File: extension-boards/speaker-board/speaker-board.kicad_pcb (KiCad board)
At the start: 2 copper layers, 60 x 40 mm, 14 parts, among them J1 Conn_02x04_Odd_Even, U1 LM386

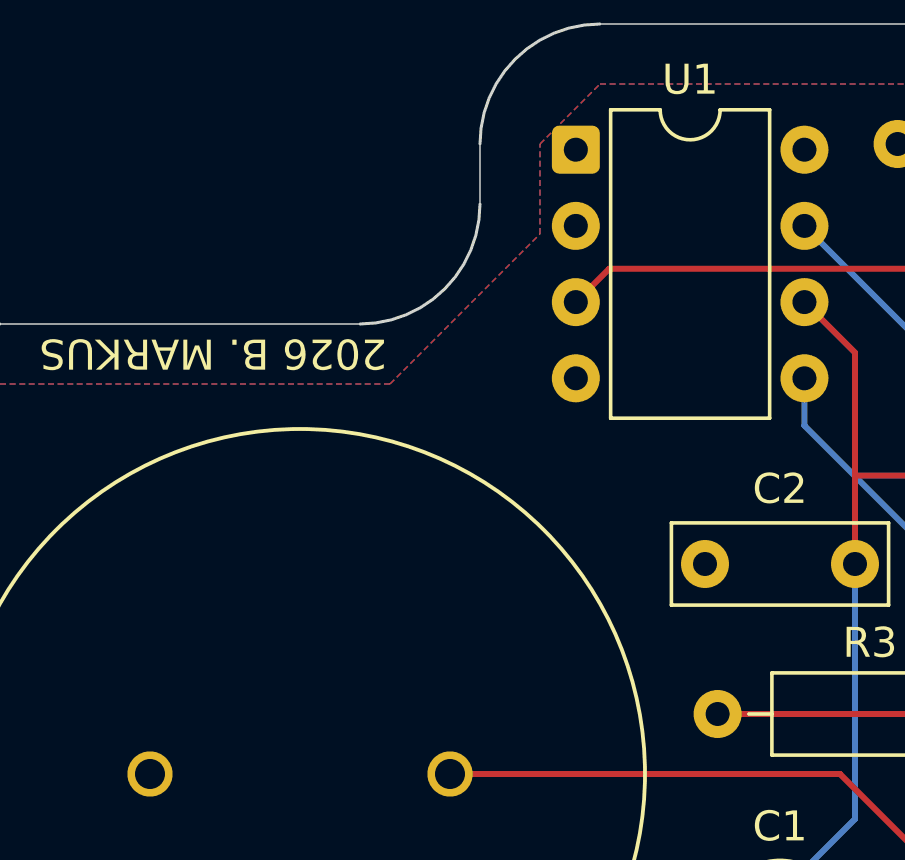
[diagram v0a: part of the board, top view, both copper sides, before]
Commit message: Schematic: Silkscreen updated on boards
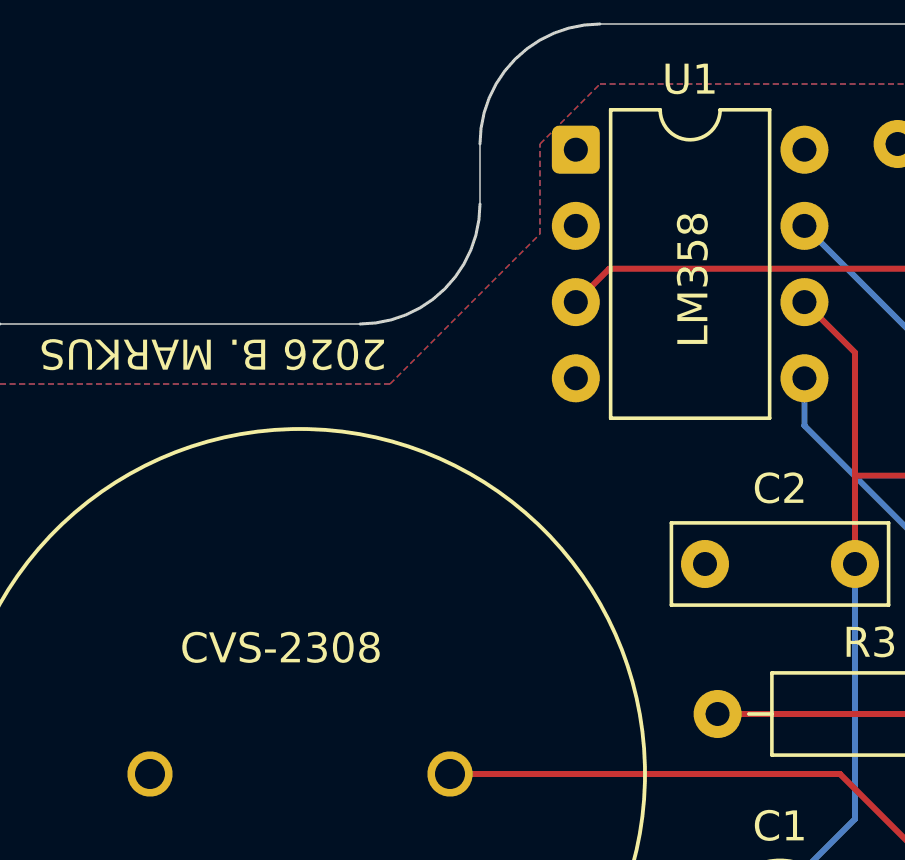
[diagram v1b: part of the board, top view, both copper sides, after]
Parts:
- R1, R2: value 330k -> 300k
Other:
- board text added: "CVS-2308"
- board text added: "LM358"
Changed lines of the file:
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@@
 			)
 		)
-		(property "Value" "330k"
+		(property "Value" "300k"
 			(at 5.08 2.37 0)
 			(layer "F.Fab")
@@
 			)
 		)
-		(property "Value" "330k"
+		(property "Value" "300k"
 			(at 5.08 2.37 0)
 			(layer "F.Fab")
@@
 		(layer "Edge.Cuts")
 	)
+	(gr_text "LM358"
+		(at 7.7 10.8 90)
+		(layer "F.SilkS")
+		(effects
+			(font
+				(size 1 1)
+				(thickness 0.15)
+			)
+			(justify left bottom)
+		)
+	)
 	(gr_text "GND"
 		(at 30.888 18.92 0)
@@
 			)
 			(justify left bottom)
+		)
+	)
+	(gr_text "CVS-2308"
+		(at -10 21.4 0)
+		(layer "F.SilkS")
+		(effects
+			(font
+				(size 1 1)
+				(thickness 0.15)
+			)
+			(justify left bottom)

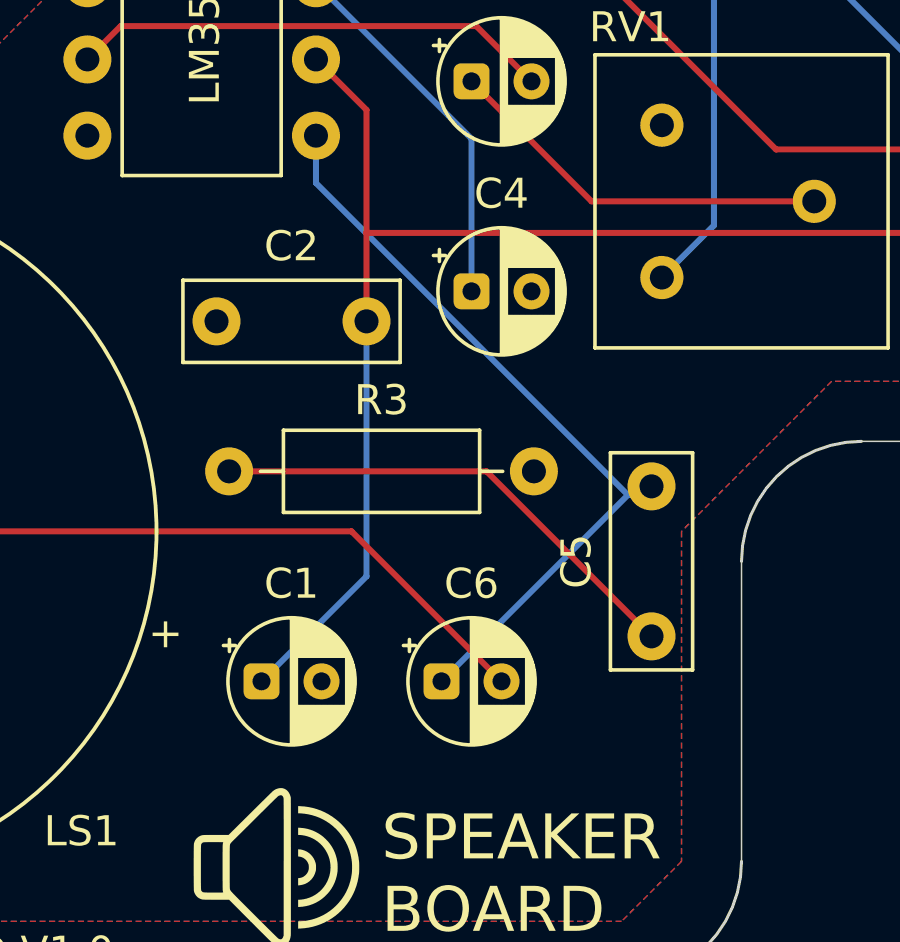
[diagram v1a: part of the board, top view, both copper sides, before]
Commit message: Footprints updated, MPLAB X IDE build configurations updated
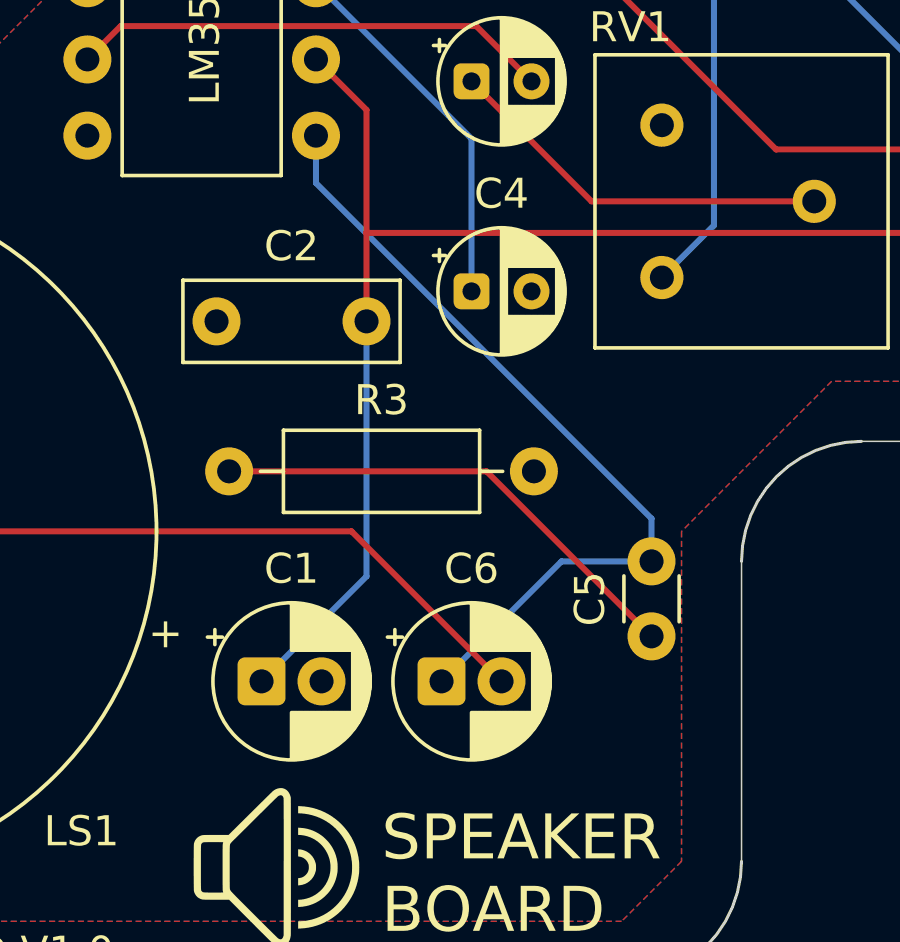
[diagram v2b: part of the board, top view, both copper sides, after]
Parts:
- C1, C6: footprint Capacitor_THT:CP_Radial_D4.0mm_P2.00mm -> Capacitor_THT:CP_Radial_D5.0mm_P2.00mm
- C5: footprint StockLib:C_100nF_L7.0mm_W2.5mm_P5.00mm -> Capacitor_THT:C_Disc_D3.0mm_W1.6mm_P2.50mm
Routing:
- net Net-(C5-Pad2): track 26.0 -> 27.5 mm
